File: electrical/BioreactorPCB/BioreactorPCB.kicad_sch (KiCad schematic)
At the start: 27 parts, among them IC1 AL5809-20P1-7, J1 61300311121, J12 Conn_02x03_Odd_Even, J2 61300311121, J3 Conn_01x05_Male, J4 Conn_01x06_Male, J6 OSTTC022162, J8 OSTTC042162, Q1 2N3905, Q2 IRF540N, U3 ATMEGA328P-AUR, Y1 16 mHz

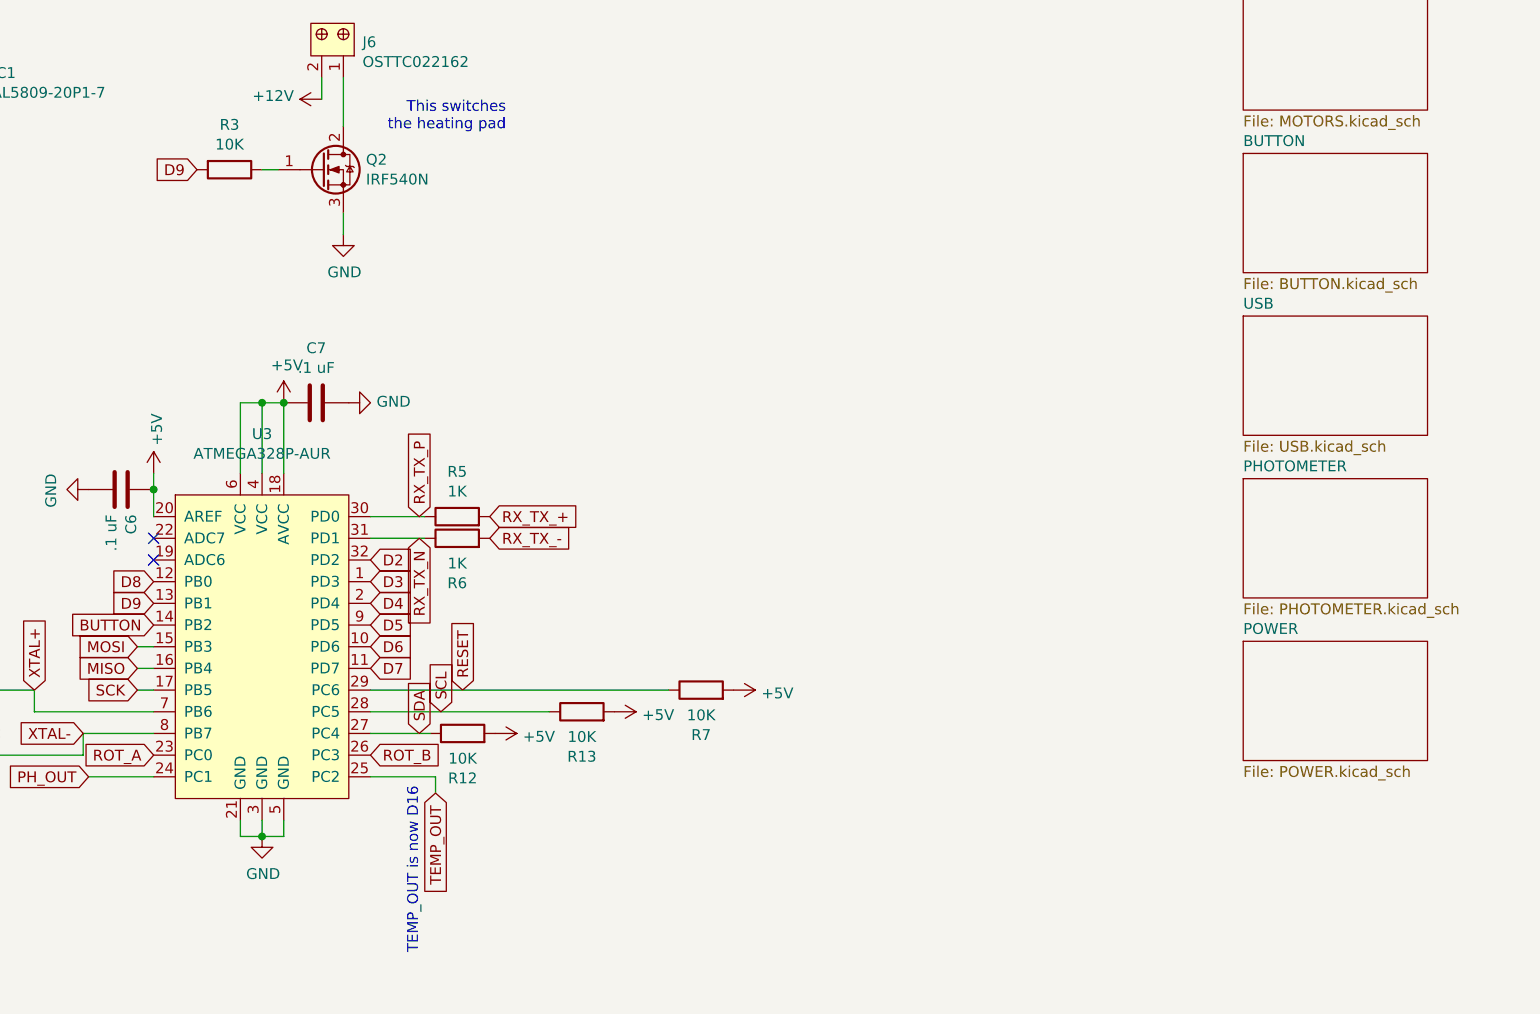
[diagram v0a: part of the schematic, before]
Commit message: Added alternate Atmega328PB 32QFN package and rerouted board to match
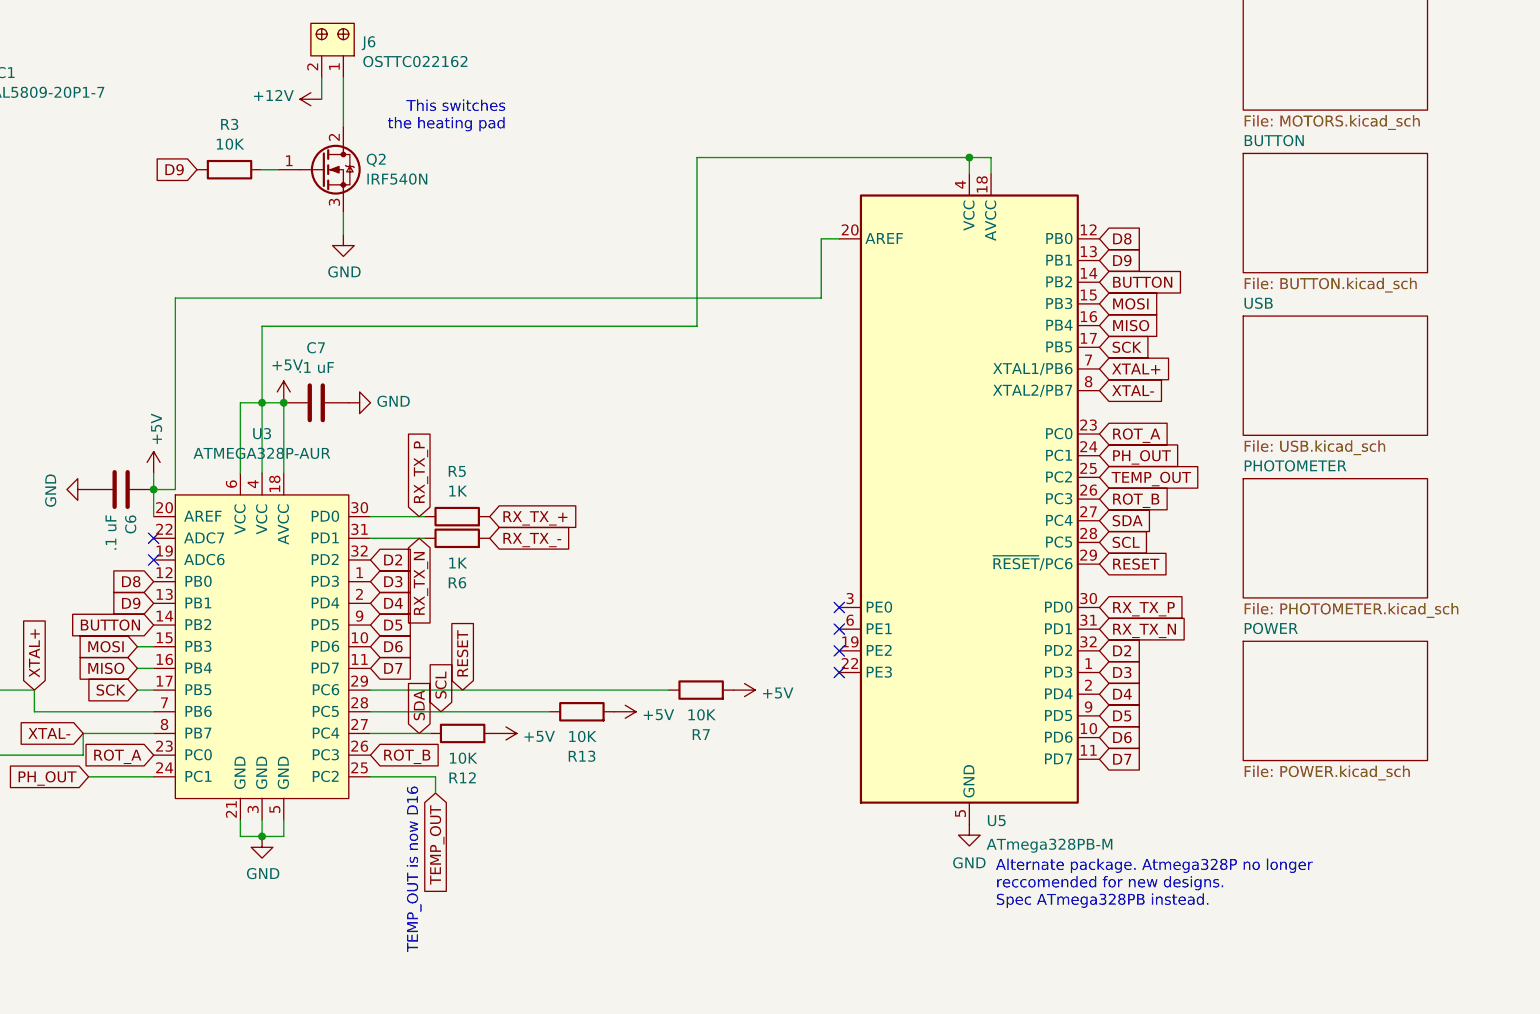
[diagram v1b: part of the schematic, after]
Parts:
- added U5: ATmega328PB-M, Package_DFN_QFN:QFN-32-1EP_5x5mm_P0.5mm_EP3.1x3.1mm, symbol MCU_Microchip_ATmega:ATmega328PB-M
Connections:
- net +5V: now also U5.18 (AVCC), U5.20 (AREF), U5.4 (VCC)
- net BUTTON: now also U5.14 (PB2)
- net D2: now also U5.32 (PD2)
- net D3: now also U5.1 (PD3)
- net D4: now also U5.2 (PD4)
- net D5: now also U5.9 (PD5)
- net D6: now also U5.10 (PD6)
- net D7: now also U5.11 (PD7)
- net D8: now also U5.12 (PB0)
- net D9: now also U5.13 (PB1)
- net GND: now also U5.21 (GND), U5.33 (GND), U5.5 (GND)
- net MISO: now also U5.16 (PB4)
- net MOSI: now also U5.15 (PB3)
- net PH_OUT: now also U5.24 (PC1)
- net RESET: now also U5.29 (~{RESET}/PC6)
- net ROT_A: now also U5.23 (PC0)
- net ROT_B: now also U5.26 (PC3)
- net RX_TX_N: now also U5.31 (PD1)
- net RX_TX_P: now also U5.30 (PD0)
- net SCK: now also U5.17 (PB5)
- net SCL: now also U5.28 (PC5)
- net SDA: now also U5.27 (PC4)
- net TEMP_OUT: now also U5.25 (PC2)
- net XTAL+: now also U5.7 (XTAL1/PB6)
- net XTAL-: now also U5.8 (XTAL2/PB7)
- no-connect marks 4 -> 8
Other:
- note added: "Alternate package. Atmega328P no longer reccomended for new designs. Spec ATmega328PB instead."

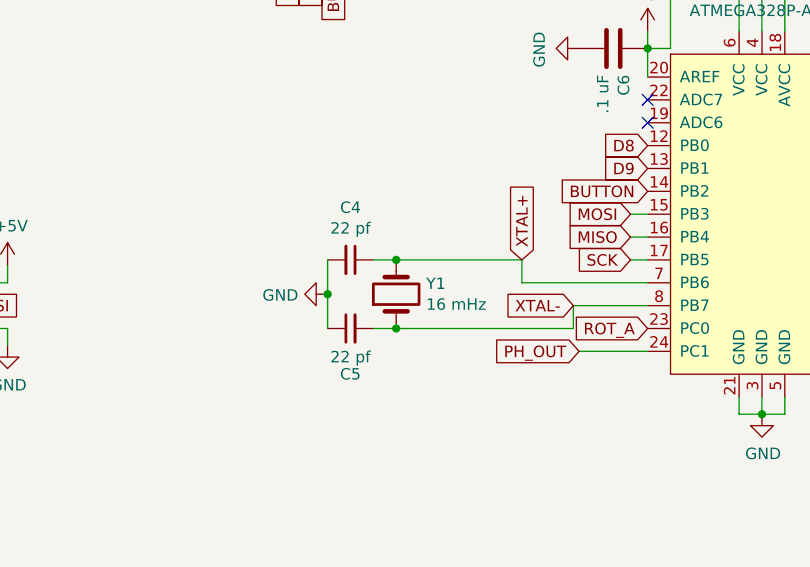
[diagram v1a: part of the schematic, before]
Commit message: Replaced through-hole crystal with SMD package and moved capacitors so they actually decouple the MCU
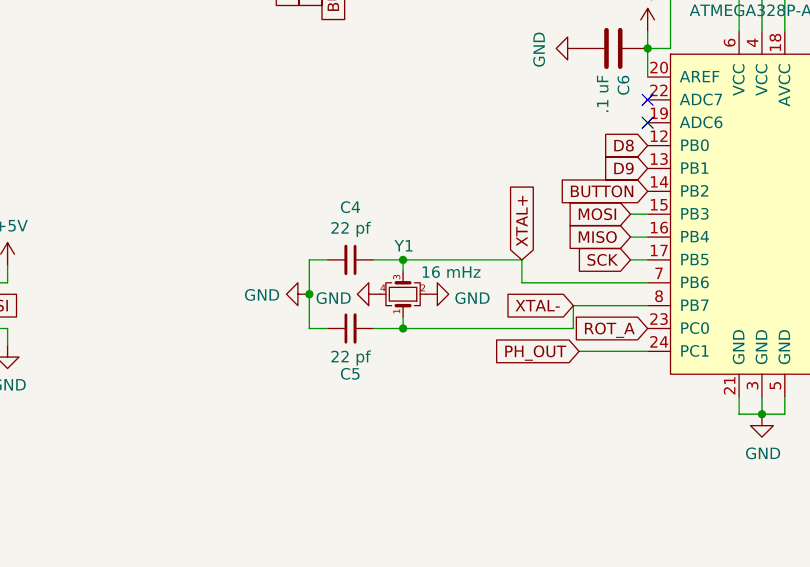
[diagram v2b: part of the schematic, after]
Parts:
- removed Y1: 16 mHz, Crystal:Crystal_HC49-U_Vertical, symbol Device:Crystal
- added Y1: 16 mHz, Crystal:Crystal_SMD_3225-4Pin_3.2x2.5mm_HandSoldering, symbol Device:Crystal_GND24_Small
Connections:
- net GND: now also Y1.2, Y1.4
- net XTAL+: now also Y1.3
- net XTAL-: now also Y1.1
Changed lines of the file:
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@@
 (kicad_sch (version 20211123) (generator eeschema)
   (paper "A4")
-  (junction (at 100.965 130.81) (diameter 0) (color 0 0 0 0)
+  (junction (at 101.727 138.43) (diameter 0) (color 0 0 0 0)
+  )
+  (junction (at 101.727 130.81) (diameter 0) (color 0 0 0 0)
   )
   (junction (at 224.4598 68.4276) (diameter 0) (color 0 0 0 0)
@@
   (junction (at 144.145 97.155) (diameter 0) (color 0 0 0 0)
   )
-  (junction (at 100.965 138.43) (diameter 0) (color 0 0 0 0)
+  (junction (at 91.313 134.62) (diameter 0) (color 0 0 0 0)
   )
   (junction (at 128.905 107.315) (diameter 0) (color 0 0 0 0)
-  )
-  (junction (at 93.345 134.62) (diameter 0) (color 0 0 0 0)
   )
   (junction (at 141.605 147.955) (diameter 0) (color 0 0 0 0)
@@
     (stroke (width 0) (type default) (color 0 0 0 0))
   )
+  (wire (pts (xy 101.727 130.81) (xy 101.727 132.08))
+    (stroke (width 0) (type default) (color 0 0 0 0))
+  )
   (wire (pts (xy 141.605 147.955) (xy 144.145 147.955))
     (stroke (width 0) (type default) (color 0 0 0 0))
@@
     (stroke (width 0) (type default) (color 0 0 0 0))
   )
+  (wire (pts (xy 101.727 137.16) (xy 101.727 138.43))
+    (stroke (width 0) (type default) (color 0 0 0 0))
+  )
   (wire (pts (xy 139.065 97.155) (xy 141.605 97.155))
     (stroke (width 0) (type default) (color 0 0 0 0))
@@
     (stroke (width 0) (type default) (color 0 0 0 0))
   )
+  (wire (pts (xy 91.313 130.81) (xy 93.345 130.81))
+    (stroke (width 0) (type default) (color 0 0 0 0))
+  )
   (wire (pts (xy 144.145 105.41) (xy 144.145 97.155))
     (stroke (width 0) (type default) (color 0 0 0 0))
   )
-  (wire (pts (xy 93.345 134.62) (xy 93.345 138.43))
+  (wire (pts (xy 91.313 130.81) (xy 91.313 134.62))
     (stroke (width 0) (type default) (color 0 0 0 0))
   )
@@
     (stroke (width 0) (type default) (color 0 0 0 0))
   )
+  (wire (pts (xy 101.727 138.43) (xy 120.65 138.43))
+    (stroke (width 0) (type default) (color 0 0 0 0))
+  )
   (wire (pts (xy 127 128.27) (xy 128.905 128.27))
     (stroke (width 0) (type default) (color 0 0 0 0))
@@
     (stroke (width 0) (type default) (color 0 0 0 0))
   )
-  (wire (pts (xy 100.965 130.81) (xy 114.935 130.81))
+  (wire (pts (xy 98.425 130.81) (xy 101.727 130.81))
     (stroke (width 0) (type default) (color 0 0 0 0))
   )
@@
     (stroke (width 0) (type default) (color 0 0 0 0))
   )
-  (wire (pts (xy 93.345 130.81) (xy 93.345 134.62))
-    (stroke (width 0) (type default) (color 0 0 0 0))
-  )
   (wire (pts (xy 144.145 97.155) (xy 141.605 97.155))
     (stroke (width 0) (type default) (color 0 0 0 0))
   )
-  (wire (pts (xy 98.425 138.43) (xy 100.965 138.43))
-    (stroke (width 0) (type default) (color 0 0 0 0))
-  )
   (wire (pts (xy 224.4598 68.4276) (xy 224.4598 70.3326))
     (stroke (width 0) (type default) (color 0 0 0 0))
@@
     (stroke (width 0) (type default) (color 0 0 0 0))
   )
-  (wire (pts (xy 98.425 130.81) (xy 100.965 130.81))
-    (stroke (width 0) (type default) (color 0 0 0 0))
-  )
   (wire (pts (xy 91.44 35.56) (xy 91.44 58.42))
     (stroke (width 0) (type default) (color 0 0 0 0))
   )
+  (wire (pts (xy 91.313 138.43) (xy 93.345 138.43))
+    (stroke (width 0) (type default) (color 0 0 0 0))
+  )
   (wire (pts (xy 80.645 53.34) (xy 85.09 53.34))
     (stroke (width 0) (type default) (color 0 0 0 0))
@@
     (stroke (width 0) (type default) (color 0 0 0 0))
   )
-  (wire (pts (xy 100.965 138.43) (xy 120.65 138.43))
+  (wire (pts (xy 98.425 138.43) (xy 101.727 138.43))
     (stroke (width 0) (type default) (color 0 0 0 0))
   )
@@
     (stroke (width 0) (type default) (color 0 0 0 0))
   )
+  (wire (pts (xy 101.727 130.81) (xy 114.935 130.81))
+    (stroke (width 0) (type default) (color 0 0 0 0))
+  )
   (wire (pts (xy 40.64 40.005) (xy 43.18 40.005))
     (stroke (width 0) (type default) (color 0 0 0 0))
@@
   )
   (wire (pts (xy 154.305 133.35) (xy 175.26 133.35))
+    (stroke (width 0) (type default) (color 0 0 0 0))
+  )
+  (wire (pts (xy 91.313 134.62) (xy 91.313 138.43))
     (stroke (width 0) (type default) (color 0 0 0 0))
   )
@@
       (effects (font (size 1.27 1.27)) hide)
     )
-  )
-  (symbol (lib_id "Device:Crystal") (at 100.965 134.62 90) (unit 1)
-    (in_bom yes) (on_board yes)
-    (property "Reference" "Y1" (id 0) (at 104.2924 133.4516 90)
-      (effects (font (size 1.27 1.27)) (justify right))
-    )
-    (property "Value" "16 mHz" (id 1) (at 104.2924 135.763 90)
-      (effects (font (size 1.27 1.27)) (justify right))
-    )
-    (property "Footprint" "Crystal:Crystal_HC49-U_Vertical" (id 2) (at 100.965 134.62 0)
-      (effects (font (size 1.27 1.27)) hide)
-    )
-    (property "Datasheet" "~" (id 3) (at 100.965 134.62 0)
-      (effects (font (size 1.27 1.27)) hide)
-    )
-    (pin "1")
-    (pin "2")
   )
   (symbol (lib_id "dk_Embedded-Microcontrollers:ATMEGA328P-AUR") (at 141.605 130.81 0) (unit 1)
@@
     (pin "2")
   )
-  (symbol (lib_id "power:GND") (at 93.345 134.62 270) (unit 1)
-    (in_bom yes) (on_board yes)
-    (property "Reference" "#PWR0156" (id 0) (at 86.995 134.62 0)
-      (effects (font (size 1.27 1.27)) hide)
-    )
-    (property "Value" "GND" (id 1) (at 90.0938 134.747 90)
+  (symbol (lib_id "power:GND") (at 91.313 134.62 270) (unit 1)
+    (in_bom yes) (on_board yes)
+    (property "Reference" "#PWR0156" (id 0) (at 84.963 134.62 0)
+      (effects (font (size 1.27 1.27)) hide)
+    )
+    (property "Value" "GND" (id 1) (at 88.0618 134.747 90)
       (effects (font (size 1.27 1.27)) (justify right))
     )
-    (property "Footprint" "" (id 2) (at 93.345 134.62 0)
-      (effects (font (size 1.27 1.27)) hide)
-    )
-    (property "Datasheet" "" (id 3) (at 93.345 134.62 0)
+    (property "Footprint" "" (id 2) (at 91.313 134.62 0)
+      (effects (font (size 1.27 1.27)) hide)
+    )
+    (property "Datasheet" "" (id 3) (at 91.313 134.62 0)
       (effects (font (size 1.27 1.27)) hide)
     )
@@
     (pin "2")
   )
+  (symbol (lib_id "power:GND") (at 104.267 134.62 90) (unit 1)
+    (in_bom yes) (on_board yes) (fields_autoplaced)
+    (property "Reference" "#PWR0164" (id 0) (at 110.617 134.62 0)
+      (effects (font (size 1.27 1.27)) hide)
+    )
+    (property "Value" "GND" (id 1) (at 107.442 135.099 90)
+      (effects (font (size 1.27 1.27)) (justify right))
+    )
+    (property "Footprint" "" (id 2) (at 104.267 134.62 0)
+      (effects (font (size 1.27 1.27)) hide)
+    )
+    (property "Datasheet" "" (id 3) (at 104.267 134.62 0)
+      (effects (font (size 1.27 1.27)) hide)
+    )
+    (pin "1")
+  )
   (symbol (lib_id "power:GND") (at 224.4598 146.5326 0) (unit 1)
     (in_bom yes) (on_board yes) (fields_autoplaced)
@@
     )
     (property "Datasheet" "" (id 3) (at 224.4598 146.5326 0)
+      (effects (font (size 1.27 1.27)) hide)
+    )
+    (pin "1")
+  )
+  (symbol (lib_id "power:GND") (at 99.187 134.62 270) (unit 1)
+    (in_bom yes) (on_board yes) (fields_autoplaced)
+    (property "Reference" "#PWR0165" (id 0) (at 92.837 134.62 0)
+      (effects (font (size 1.27 1.27)) hide)
+    )
+    (property "Value" "GND" (id 1) (at 96.0121 135.099 90)
+      (effects (font (size 1.27 1.27)) (justify right))
+    )
+    (property "Footprint" "" (id 2) (at 99.187 134.62 0)
+      (effects (font (size 1.27 1.27)) hide)
+    )
+    (property "Datasheet" "" (id 3) (at 99.187 134.62 0)
       (effects (font (size 1.27 1.27)) hide)
     )
@@
     (pin "9")
   )
+  (symbol (lib_id "Device:Crystal_GND24_Small") (at 101.727 134.62 90) (unit 1)
+    (in_bom yes) (on_board yes)
+    (property "Reference" "Y1" (id 0) (at 101.854 129.286 90))
+    (property "Value" "16 mHz" (id 1) (at 107.061 132.207 90))
+    (property "Footprint" "Crystal:Crystal_SMD_3225-4Pin_3.2x2.5mm_HandSoldering" (id 2) (at 101.727 134.62 0)
+      (effects (font (size 1.27 1.27)) hide)
+    )
+    (property "Datasheet" "~" (id 3) (at 101.727 134.62 0)
+      (effects (font (size 1.27 1.27)) hide)
+    )
+    (pin "1")
+    (pin "2")
+    (pin "3")
+    (pin "4")
+  )
   (symbol (lib_id "Device:R") (at 165.1 135.89 90) (unit 1)
     (in_bom yes) (on_board yes)
@@
       (reference "#PWR0163") (unit 1) (value "+5V") (footprint "")
     )
+    (path "/09823e9b-40eb-4e18-b8b3-388b48b7f596"
+      (reference "#PWR0164") (unit 1) (value "GND") (footprint "")
+    )
+    (path "/7f52b226-d041-4455-8619-ed92acec4a59"
+      (reference "#PWR0165") (unit 1) (value "GND") (footprint "")
+    )
     (path "/00000000-0000-0000-0000-00006200bc19/00000000-0000-0000-0000-000062057055"
       (reference "A1") (unit 1) (value "Pololu_Breakout_A4988") (footprint "Module:Pololu_Breakout-16_15.2x20.3mm")
@@
       (reference "U5") (unit 1) (value "ATmega328PB-M") (footprint "Package_DFN_QFN:QFN-32-1EP_5x5mm_P0.5mm_EP3.1x3.1mm")
     )
-    (path "/00000000-0000-0000-0000-000061d3e37a"
-      (reference "Y1") (unit 1) (value "16 mHz") (footprint "Crystal:Crystal_HC49-U_Vertical")
-    )
-  )
+    (path "/e34f1c24-1183-4266-942c-fcb14ff686e5"
+      (reference "Y1") (unit 1) (value "16 mHz") (footprint "Crystal:Crystal_SMD_3225-4Pin_3.2x2.5mm_HandSoldering")
+    )
+  )

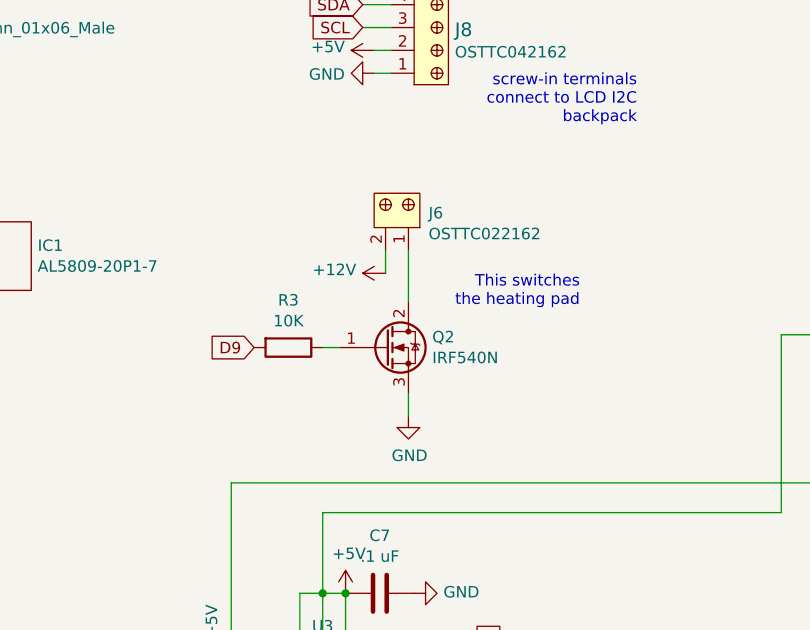
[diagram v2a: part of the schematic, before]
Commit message: changed MOSFET to PFET and made the heater switched by a high-side switch
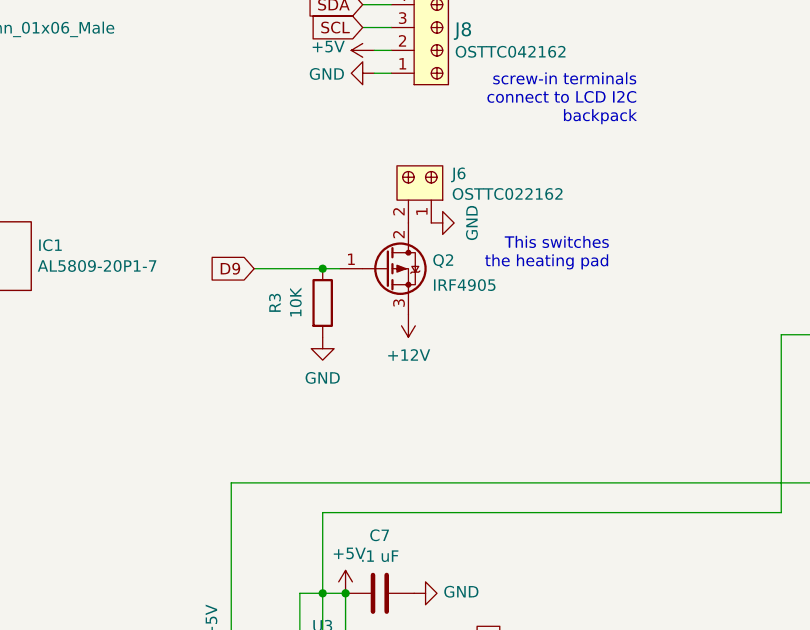
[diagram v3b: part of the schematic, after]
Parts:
- removed Q2: IRF540N, Package_TO_SOT_THT:TO-220-3_Vertical, symbol Transistor_FET:IRF540N
- added Q2: IRF4905, Package_TO_SOT_THT:TO-262-3_Vertical, symbol Transistor_FET:IRF4905
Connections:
- net +12V: now also Q2.3 (S); no longer J6.2
- net D9: now also R3.1, Q2.1 (G); no longer R3.2
- net GND: now also J6.1, R3.2
- new net: J6.2, Q2.2 (D)
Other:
- moved on the sheet: J6, R3
